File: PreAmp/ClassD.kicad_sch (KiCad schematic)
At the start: 41 parts, among them J1 Conn_01x02_Pin, J2 Conn_01x02_Pin, J3 Conn_01x03, U1 L78L09_TO92, U2 LM358, U3 TL494

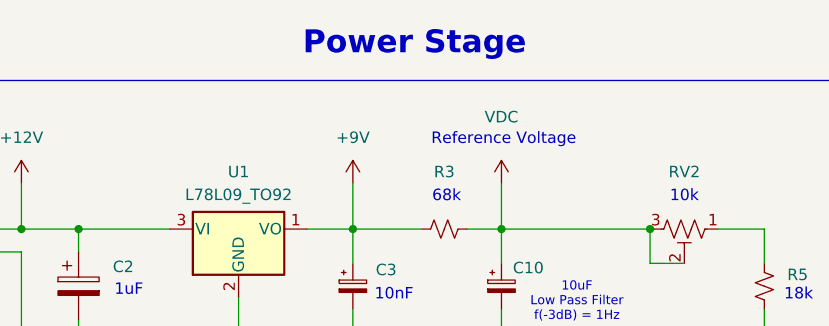
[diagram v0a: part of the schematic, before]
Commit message: Renamed pre amp input regulation
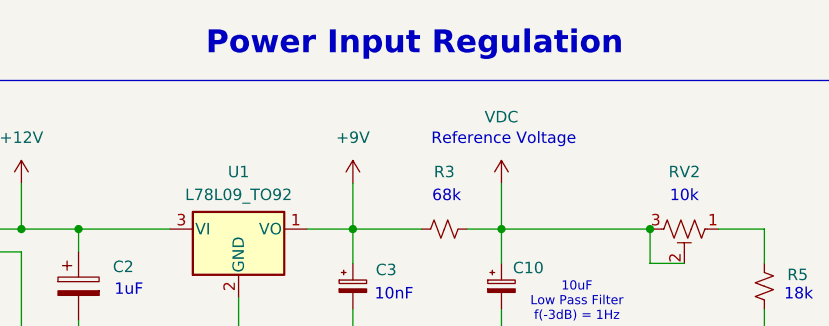
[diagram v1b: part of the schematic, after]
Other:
- note added: "Power Input Regulation"
- note removed: "Power Stage"
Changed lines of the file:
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@@
 		)
 	)
-	(text "Power Stage"
+	(text "Power Input Regulation"
 		(exclude_from_sim no)
 		(at 80.518 17.526 0)

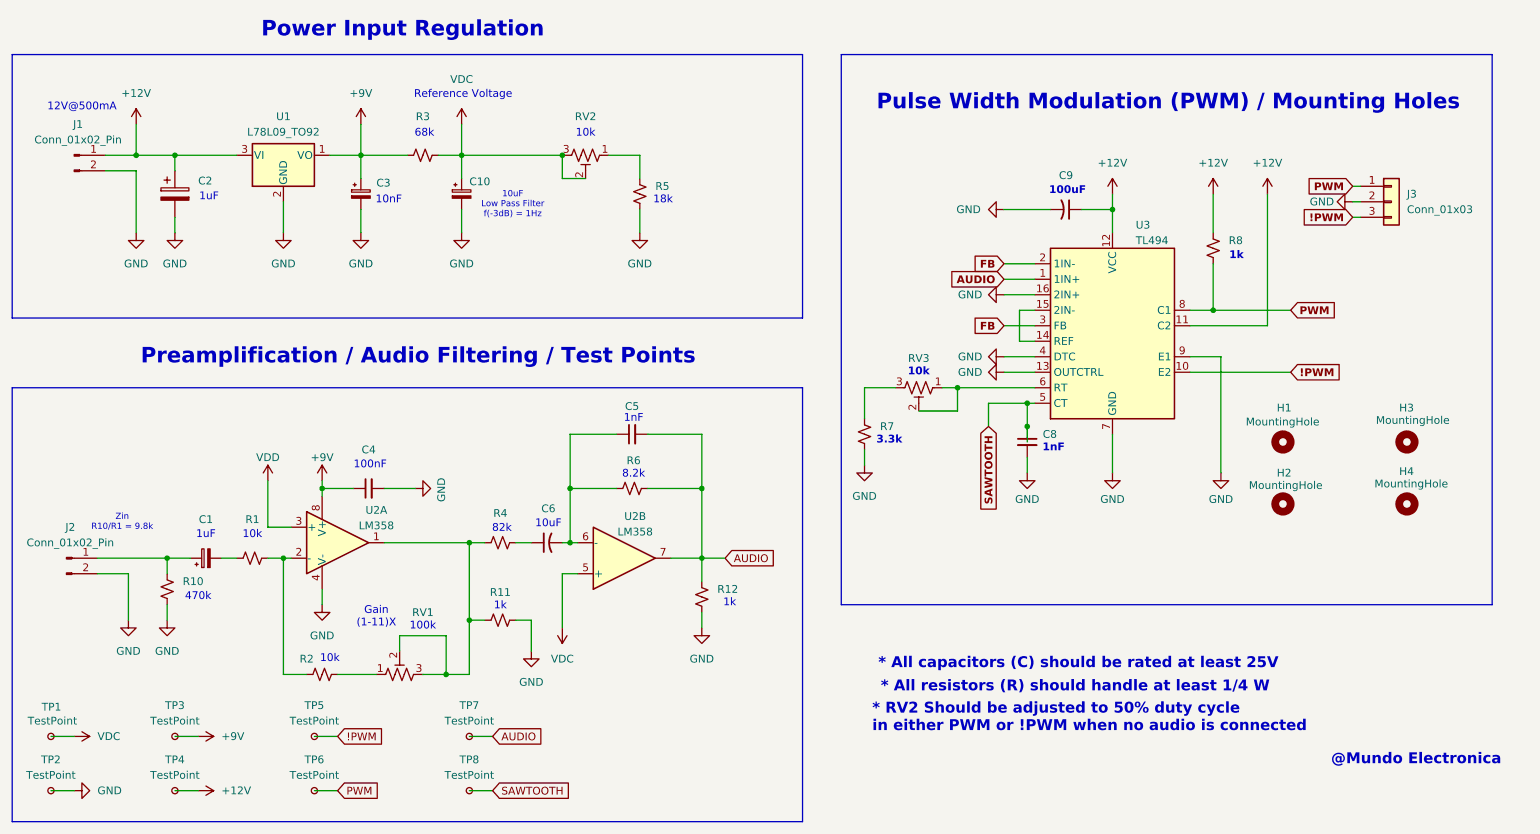
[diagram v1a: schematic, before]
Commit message: Assigned footprints to all components in Pre Amplification Stage
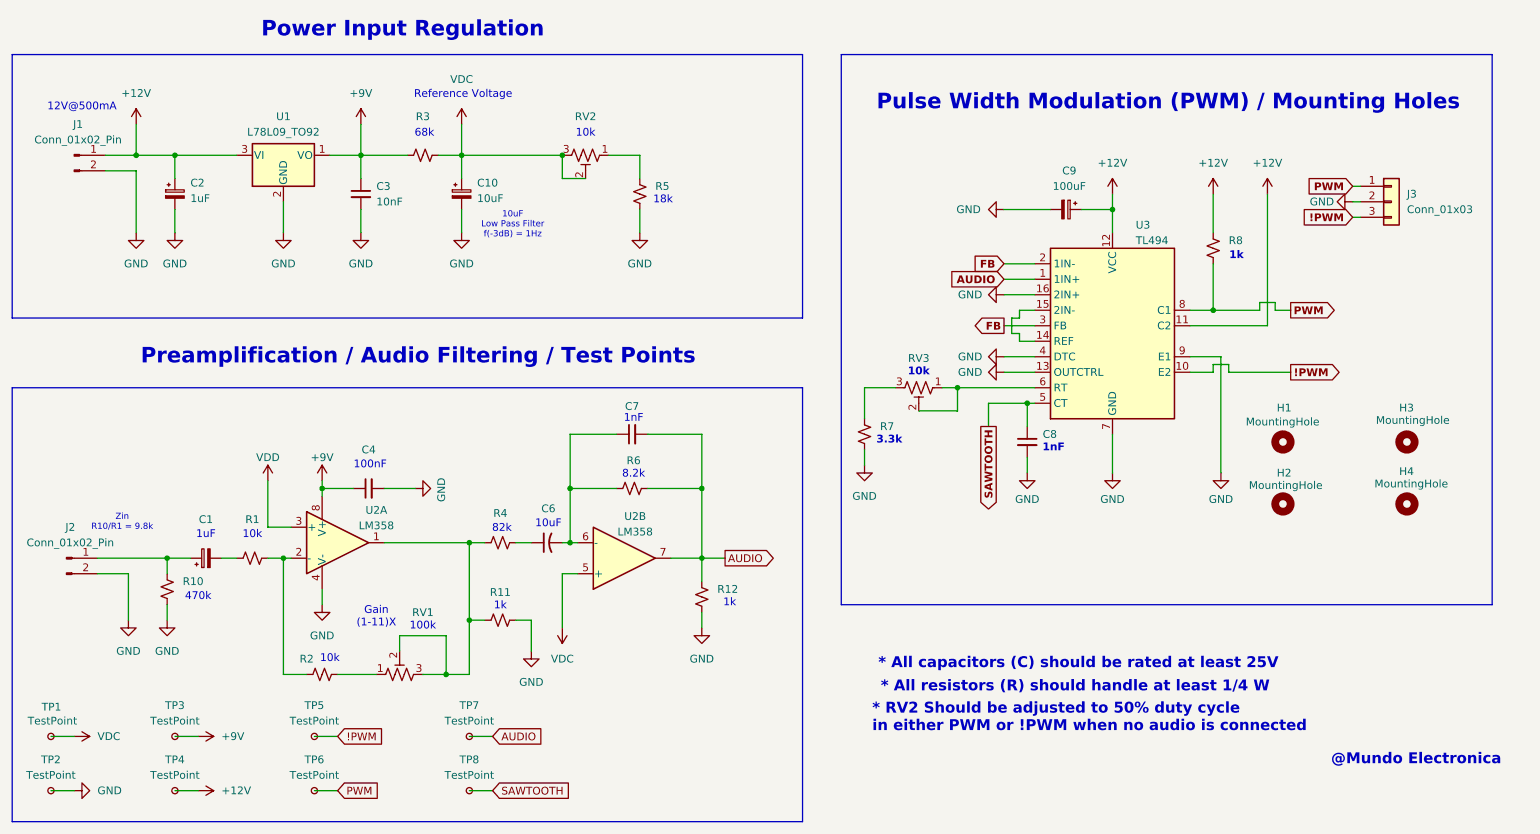
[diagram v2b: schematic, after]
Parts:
- removed C2: C_Polarized, symbol Device:C_Polarized
- removed C3: C_Polarized_Small, symbol Device:C_Polarized_Small
- removed C9: C_Small_US, symbol Device:C_Small_US
- added C2: 1uF, Capacitor_THT:CP_Radial_D5.0mm_P2.00mm, symbol Device:C_Polarized_Small
- added C3: 10nF, Capacitor_THT:C_Disc_D3.8mm_W2.6mm_P2.50mm, symbol Device:C_Small
- added C9: 100uF, Capacitor_THT:CP_Radial_D8.0mm_P3.50mm, symbol Device:C_Polarized_Small
- C1, C6: footprint (none) -> Capacitor_THT:CP_Radial_D5.0mm_P2.00mm
- C10: value C_Polarized_Small -> 10uF; footprint (none) -> Capacitor_THT:CP_Radial_D5.0mm_P2.00mm
- C4: footprint (none) -> Capacitor_THT:C_Disc_D5.0mm_W2.5mm_P5.00mm
- C7: renamed from C5; footprint (none) -> Capacitor_THT:C_Disc_D3.8mm_W2.6mm_P2.50mm
- C8: footprint (none) -> Capacitor_THT:C_Disc_D3.8mm_W2.6mm_P2.50mm
- H1, H2, H3, H4: footprint (none) -> MountingHole:MountingHole_3.2mm_M3_Pad_Via
- J1: footprint (none) -> Connector_BarrelJack:BarrelJack_GCT_DCJ200-10-A_Horizontal
- J2, J3: footprint (none) -> Connector_JST:JST_XH_B3B-XH-A_1x03_P2.50mm_Vertical
- R1, R10, R11, R12, R2, R3, R4, R5, R6, R7, R8: footprint (none) -> Resistor_THT:R_Axial_DIN0204_L3.6mm_D1.6mm_P7.62mm_Horizontal
- RV1, RV2, RV3: footprint (none) -> Potentiometer_THT:Potentiometer_Bourns_3296W_Vertical
- TP1, TP2, TP3, TP4, TP5, TP6, TP7, TP8: footprint (none) -> TestPoint:TestPoint_THTPad_D2.0mm_Drill1.0mm
- U1: footprint Package_TO_SOT_THT:TO-92_Inline -> Package_TO_SOT_THT:TO-92_Inline_Wide
- U2: footprint (none) -> Package_DIP:DIP-8_W7.62mm_Socket
- U3: footprint (none) -> Package_DIP:DIP-18_W7.62mm_Socket
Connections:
- net +12V: now also C2.1, C9.1
- net +9V: now also C3.1
- net GND: now also C2.2, C3.2, C9.2
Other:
- note removed: "100uF"
- note removed: "10nF"

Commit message: Fixed audio jack to 2 pins
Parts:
- J2: footprint Connector_JST:JST_XH_B3B-XH-A_1x03_P2.50mm_Vertical -> Connector_JST:JST_XH_B2B-XH-A_1x02_P2.50mm_Vertical
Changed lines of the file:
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@@
 			)
 		)
-		(property "Footprint" "Connector_JST:JST_XH_B3B-XH-A_1x03_P2.50mm_Vertical"
+		(property "Footprint" "Connector_JST:JST_XH_B2B-XH-A_1x02_P2.50mm_Vertical"
 			(at 25.4 104.14 0)
 			(effects

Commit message: Added pictures, and write-up
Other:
- note added: "F=1/(2πRC)"
- note added: "~ 15.9Hz"
- note removed: "82k"
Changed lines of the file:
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@@
+		)
+	)
+	(text "~ 15.9Hz"
+		(exclude_from_sim no)
+		(at 50.546 115.824 0)
+		(effects
+			(font
+				(size 1.27 1.27)
+			)
 		)
 	)
@@
 		)
 	)
+	(text "F=1/(2πRC)"
+		(exclude_from_sim no)
+		(at 51.816 113.284 0)
+		(effects
+			(font
+				(size 1.27 1.27)
+			)
+		)
+	)
 	(text "@Mundo Electronica"
 		(exclude_from_sim no)
@@
 		)
 	)
-	(text "82k"
+	(text "8.2k"
 		(exclude_from_sim no)
 		(at 96.774 99.314 0)

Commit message: Fixed gain on second op-amp
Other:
- note removed: "10uF"
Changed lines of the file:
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@@
 		)
 	)
-	(text "10uF"
+	(text "1uF"
 		(exclude_from_sim no)
 		(at 104.394 98.552 0)

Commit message: Fixed R9 and pdf
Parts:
- added R9: 1k, symbol Device:R_Small_US
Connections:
- net !PWM: now also R9.1
- net GND: now also R9.2
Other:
- moved on the sheet: H1, H2, H3, H4
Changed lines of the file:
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@@
 	)
 	(junction
+		(at 220.218 73.66)
+		(diameter 0)
+		(color 0 0 0 0)
+	)
+	(junction
 		(at 73.66 38.1)
 		(diameter 0)
@@
 	(wire
 		(pts
+			(xy 220.218 73.66) (xy 220.218 75.184)
+		)
+		(stroke
+			(width 0)
+			(type default)
+		)
+	)
+	(wire
+		(pts
 			(xy 223.52 63.5) (xy 226.06 63.5)
 		)
@@
 	(wire
 		(pts
+			(xy 220.218 73.66) (xy 226.06 73.66)
+		)
+		(stroke
+			(width 0)
+			(type default)
+		)
+	)
+	(wire
+		(pts
 			(xy 43.18 142.24) (xy 46.99 142.24)
 		)
@@
 	(wire
 		(pts
-			(xy 215.9 73.66) (xy 226.06 73.66)
+			(xy 215.9 73.66) (xy 220.218 73.66)
 		)
 		(stroke
@@
 	(wire
 		(pts
+			(xy 220.218 80.264) (xy 220.218 81.534)
+		)
+		(stroke
+			(width 0)
+			(type default)
+		)
+	)
+	(wire
+		(pts
 			(xy 36.83 40.64) (xy 36.83 50.8)
 		)
@@
 	)
 	(symbol
+		(lib_id "power:GND")
+		(at 220.218 81.534 0)
+		(unit 1)
+		(exclude_from_sim no)
+		(in_bom yes)
+		(on_board yes)
+		(dnp no)
+		(fields_autoplaced yes)
+		(property "Reference" "#PWR035"
+			(at 220.218 87.884 0)
+			(effects
+				(font
+					(size 1.27 1.27)
+				)
+				(hide yes)
+			)
+		)
+		(property "Value" "GND"
+			(at 220.218 86.36 0)
+			(effects
+				(font
+					(size 1.27 1.27)
+				)
+			)
+		)
+		(property "Footprint" ""
+			(at 220.218 81.534 0)
+			(effects
+				(font
+					(size 1.27 1.27)
+				)
+				(hide yes)
+			)
+		)
+		(property "Datasheet" ""
+			(at 220.218 81.534 0)
+			(effects
+				(font
+					(size 1.27 1.27)
+				)
+				(hide yes)
+			)
+		)
+		(property "Description" "Power symbol creates a global label with name \"GND\" , ground"
+			(at 220.218 81.534 0)
+			(effects
+				(font
+					(size 1.27 1.27)
+				)
+				(hide yes)
+			)
+		)
+		(pin "1"
+		)
+		(instances
+			(project ""
+				(path "/fdc31853-4cdf-4258-8ce4-3d650134335c"
+					(reference "#PWR035")
+					(unit 1)
+				)
+			)
+		)
+	)
+	(symbol
 		(lib_id "Device:C_Small")
 		(at 118.11 83.82 90)
@@
 	(symbol
 		(lib_id "Mechanical:MountingHole")
-		(at 245.11 95.25 0)
+		(at 245.364 105.664 0)
 		(unit 1)
 		(exclude_from_sim no)
@@
 		(dnp no)
 		(property "Reference" "H4"
-			(at 243.84 89.916 0)
+			(at 244.094 100.33 0)
 			(effects
 				(font
@@
 		)
 		(property "Value" "MountingHole"
-			(at 239.776 91.948 0)
+			(at 240.03 102.362 0)
 			(effects
 				(font
@@
 		)
 		(property "Footprint" "MountingHole:MountingHole_3.2mm_M3_Pad_Via"
-			(at 245.11 95.25 0)
+			(at 245.364 105.664 0)
 			(effects
 				(font
@@
 		)
 		(property "Datasheet" "~"
-			(at 245.11 95.25 0)
+			(at 245.364 105.664 0)
 			(effects
 				(font
@@
 		)
 		(property "Description" "Mounting Hole without connection"
-			(at 245.11 95.25 0)
+			(at 245.364 105.664 0)
 			(effects
 				(font
@@
 	(symbol
 		(lib_id "Mechanical:MountingHole")
-		(at 224.79 85.09 0)
+		(at 225.044 95.504 0)
 		(unit 1)
 		(exclude_from_sim no)
@@
 		(dnp no)
 		(property "Reference" "H1"
-			(at 223.774 79.502 0)
+			(at 224.028 89.916 0)
 			(effects
 				(font
@@
 		)
 		(property "Value" "MountingHole"
-			(at 218.694 81.788 0)
+			(at 218.948 92.202 0)
 			(effects
 				(font
@@
 		)
 		(property "Footprint" "MountingHole:MountingHole_3.2mm_M3_Pad_Via"
-			(at 224.79 85.09 0)
+			(at 225.044 95.504 0)
 			(effects
 				(font
@@
 		)
 		(property "Datasheet" "~"
-			(at 224.79 85.09 0)
+			(at 225.044 95.504 0)
 			(effects
 				(font
@@
 		)
 		(property "Description" "Mounting Hole without connection"
-			(at 224.79 85.09 0)
+			(at 225.044 95.504 0)
 			(effects
 				(font
@@
 	(symbol
 		(lib_id "Mechanical:MountingHole")
-		(at 245.11 85.09 0)
+		(at 245.364 95.504 0)
 		(unit 1)
 		(exclude_from_sim no)
@@
 		(dnp no)
 		(property "Reference" "H3"
-			(at 243.84 79.502 0)
+			(at 244.094 89.916 0)
 			(effects
 				(font
@@
 		)
 		(property "Value" "MountingHole"
-			(at 240.03 81.534 0)
+			(at 240.284 91.948 0)
 			(effects
 				(font
@@
 		)
 		(property "Footprint" "MountingHole:MountingHole_3.2mm_M3_Pad_Via"
-			(at 245.11 85.09 0)
+			(at 245.364 95.504 0)
 			(effects
 				(font
@@
 		)
 		(property "Datasheet" "~"
-			(at 245.11 85.09 0)
+			(at 245.364 95.504 0)
 			(effects
 				(font
@@
 		)
 		(property "Description" "Mounting Hole without connection"
-			(at 245.11 85.09 0)
+			(at 245.364 95.504 0)
 			(effects
 				(font
@@
 	)
 	(symbol
+		(lib_id "Device:R_Small_US")
+		(at 220.218 77.724 0)
+		(unit 1)
+		(exclude_from_sim no)
+		(in_bom yes)
+		(on_board yes)
+		(dnp no)
+		(fields_autoplaced yes)
+		(property "Reference" "R9"
+			(at 222.25 76.4539 0)
+			(effects
+				(font
+					(size 1.27 1.27)
+				)
+				(justify left)
+			)
+		)
+		(property "Value" "1k"
+			(at 222.25 78.9939 0)
+			(effects
+				(font
+					(size 1.27 1.27)
+				)
+				(justify left)
+			)
+		)
+		(property "Footprint" ""
+			(at 220.218 77.724 0)
+			(effects
+				(font
+					(size 1.27 1.27)
+				)
+				(hide yes)
+			)
+		)
+		(property "Datasheet" "~"
+			(at 220.218 77.724 0)
+			(effects
+				(font
+					(size 1.27 1.27)
+				)
+				(hide yes)
+			)
+		)
+		(property "Description" "Resistor, small US symbol"
+			(at 220.218 77.724 0)
+			(effects
+				(font
+					(size 1.27 1.27)
+				)
+				(hide yes)
+			)
+		)
+		(pin "2"
+		)
+		(pin "1"
+		)
+		(instances
+			(project ""
+				(path "/fdc31853-4cdf-4258-8ce4-3d650134335c"
+					(reference "R9")
+					(unit 1)
+				)
+			)
+		)
+	)
+	(symbol
 		(lib_id "Amplifier_Operational:LM358")
 		(at 116.84 104.14 0)
@@
 	(symbol
 		(lib_id "Mechanical:MountingHole")
-		(at 224.79 95.25 90)
+		(at 225.044 105.664 90)
 		(unit 1)
 		(exclude_from_sim no)
@@
 		(dnp no)
 		(property "Reference" "H2"
-			(at 223.774 90.17 90)
+			(at 224.028 100.584 90)
 			(effects
 				(font
@@
 		)
 		(property "Value" "MountingHole"
-			(at 219.202 92.202 90)
+			(at 219.456 102.616 90)
 			(effects
 				(font
@@
 		)
 		(property "Footprint" "MountingHole:MountingHole_3.2mm_M3_Pad_Via"
-			(at 224.79 95.25 0)
+			(at 225.044 105.664 0)
 			(effects
 				(font
@@
 		)
 		(property "Datasheet" "~"
-			(at 224.79 95.25 0)
+			(at 225.044 105.664 0)
 			(effects
 				(font
@@
 		)
 		(property "Description" "Mounting Hole without connection"
-			(at 224.79 95.25 0)
+			(at 225.044 105.664 0)
 			(effects
 				(font
